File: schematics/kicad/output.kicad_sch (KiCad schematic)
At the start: 9 parts, among them U1 BT458, U2 HM53461, U3 HM53461, U4 HM53461, U5 HM53461, U6 HM53461, U7 HM53461, U8 HM53461, U9 HM53461

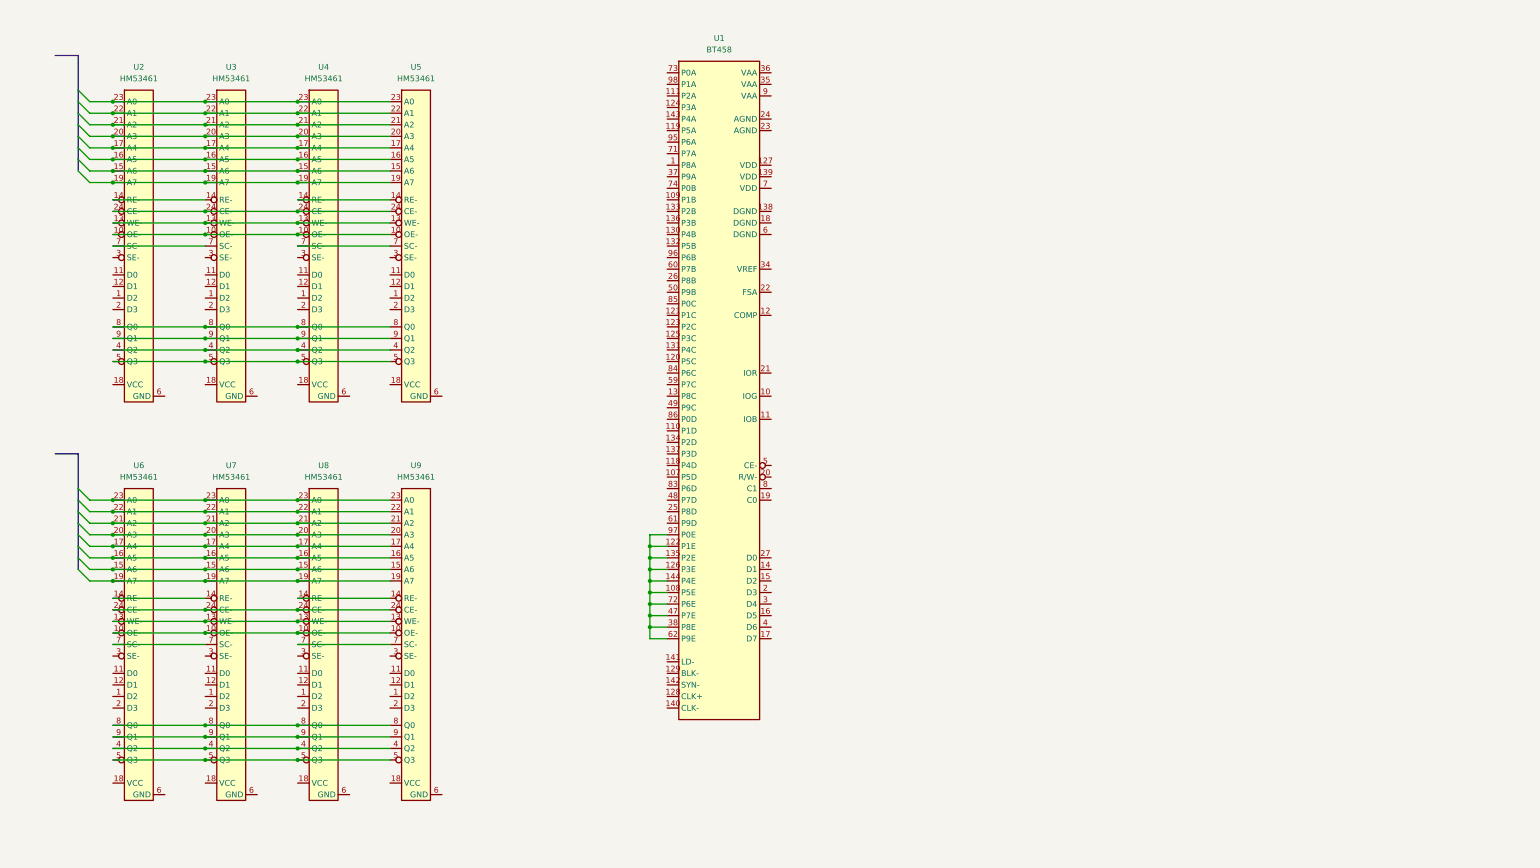
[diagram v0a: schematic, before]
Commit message: Fill in more output section
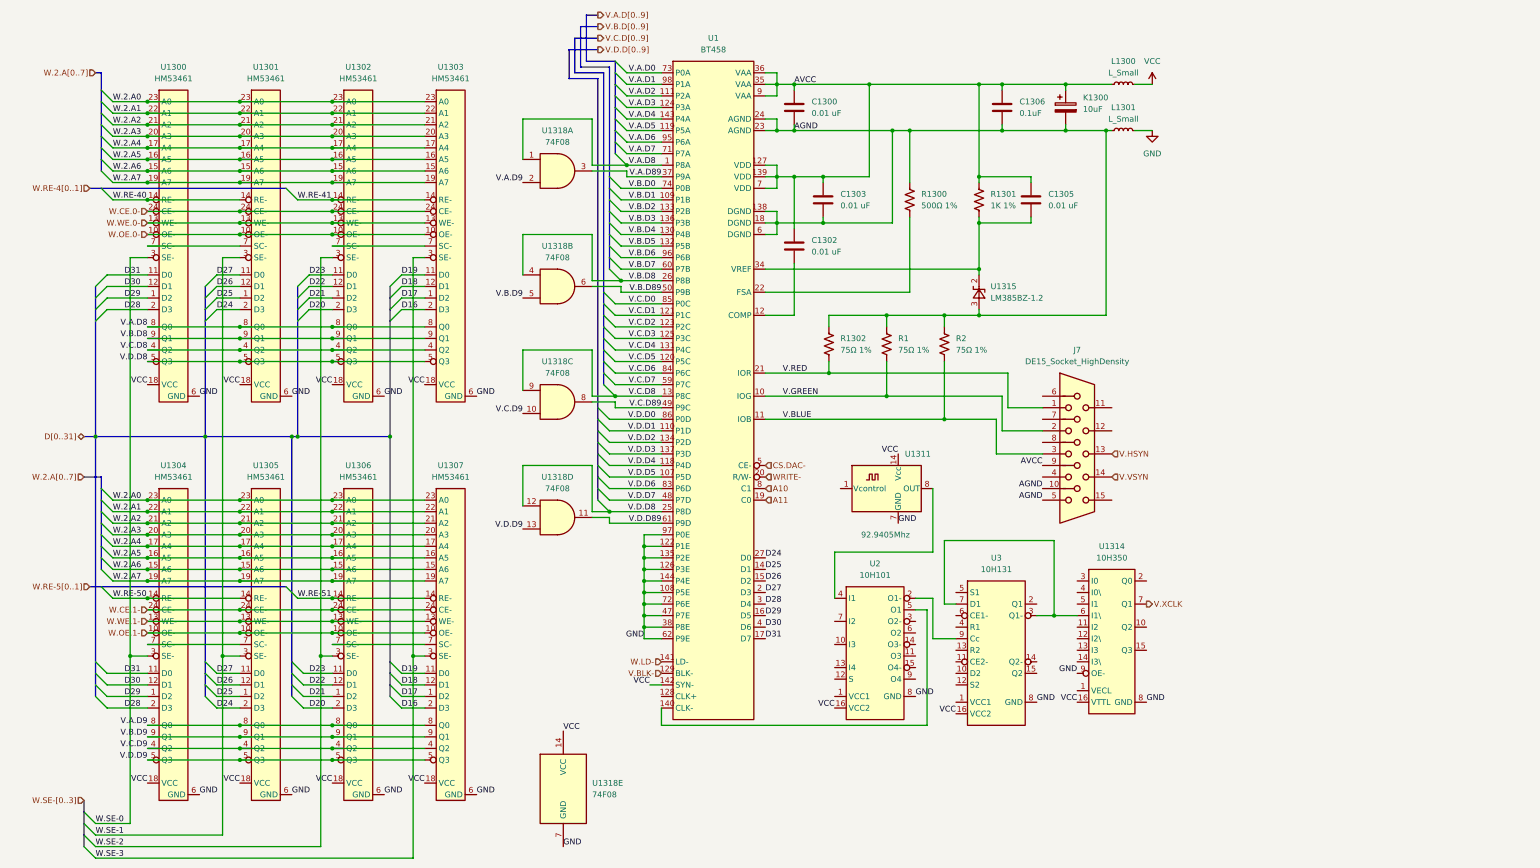
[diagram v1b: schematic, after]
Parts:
- added C1300, C1302, C1303, C1305: 0.01 uF, symbol Device:C
- added C1306: 0.1uF, symbol Device:C
- added J7: DE15_Socket_HighDensity, symbol Connector:DE15_Socket_HighDensity
- added K1300: 10uF, symbol Device:C_Polarized
- added L1300, L1301: L_Small, symbol Device:L_Small
- added R1, R1302, R2: 75Ω 1%, symbol Device:R_US
- added R1300: 500Ω 1%, symbol Device:R_US
- added R1301: 1K 1%, symbol Device:R_US
- added U1311: 92.9405Mhz, Oscillator:Oscillator_DIP-14, symbol Oscillator:OCXO-14
- added U1314: 10H350, Package_DIP:DIP-16_W7.62mm, symbol cg4:10H350
- added U1315: LM385BZ-1.2, Package_TO_SOT_THT:TO-92_Inline, symbol Reference_Voltage:LM385BZ-1.2
- added U1318: 74F08, symbol 74xx:74LS08
- added U2: 10H101, Package_DIP:DIP-16_W7.62mm, symbol cg4:10H101
- added U3: 10H131, Package_DIP:DIP-16_W7.62mm, symbol cg4:10H131
- renumbered U2 to U1300, U3 to U1301, U4 to U1302, U5 to U1303, U6 to U1304, U7 to U1305, U8 to U1306, U9 to U1307
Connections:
- net D25: now reaches U1305.1 (D2)
- net D25: now also U1.14 (D1), U1301.1 (D2)
- net W.OE.1-: now reaches U1304.10 (OE-), U1305.10 (OE-), U1306.10 (OE-), U1307.10 (OE-)
- net D27: now reaches U1305.11 (D0)
- net D27: now also U1.2 (D3), U1301.11 (D0)
- net D26: now reaches U1305.12 (D1)
- net D26: now also U1.15 (D2), U1301.12 (D1)
- net W.WE.1-: now reaches U1304.13 (WE-), U1305.13 (WE-), U1306.13 (WE-), U1307.13 (WE-)
- net W.RE-50: now reaches U1304.14 (RE-), U1305.14 (RE-)
- net W.2.A6: now reaches U1304.15 (A6), U1305.15 (A6), U1306.15 (A6), U1307.15 (A6)
- net W.2.A6: now also U1300.15 (A6), U1301.15 (A6), U1302.15 (A6), U1303.15 (A6)
- net W.2.A5: now reaches U1304.16 (A5), U1305.16 (A5), U1306.16 (A5), U1307.16 (A5)
- net W.2.A5: now also U1300.16 (A5), U1301.16 (A5), U1302.16 (A5), U1303.16 (A5)
- net W.2.A4: now reaches U1304.17 (A4), U1305.17 (A4), U1306.17 (A4), U1307.17 (A4)
- net W.2.A4: now also U1300.17 (A4), U1301.17 (A4), U1302.17 (A4), U1303.17 (A4)
- net VCC: now reaches U1305.18 (VCC)
- net VCC: now also U1.142 (SYN-), U1300.18 (VCC), U1301.18 (VCC), U1302.18 (VCC), U1303.18 (VCC), U1304.18 (VCC), U1306.18 (VCC), U1307.18 (VCC), L1300.2, U1311.14 (Vcc), U1314.16 (VTTL), U1318.14 (VCC), U2.16 (VCC2), U3.16 (VCC2)
- net W.2.A7: now reaches U1304.19 (A7), U1305.19 (A7), U1306.19 (A7), U1307.19 (A7)
- net W.2.A7: now also U1300.19 (A7), U1301.19 (A7), U1302.19 (A7), U1303.19 (A7)
- net D24: now reaches U1305.2 (D3)
- net D24: now also U1.27 (D0), U1301.2 (D3)
- net W.2.A3: now reaches U1304.20 (A3), U1305.20 (A3), U1306.20 (A3), U1307.20 (A3)
- net W.2.A3: now also U1300.20 (A3), U1301.20 (A3), U1302.20 (A3), U1303.20 (A3)
- net W.2.A2: now reaches U1304.21 (A2), U1305.21 (A2), U1306.21 (A2), U1307.21 (A2)
- net W.2.A2: now also U1300.21 (A2), U1301.21 (A2), U1302.21 (A2), U1303.21 (A2)
- net W.2.A1: now reaches U1304.22 (A1), U1305.22 (A1), U1306.22 (A1), U1307.22 (A1)
- net W.2.A1: now also U1300.22 (A1), U1301.22 (A1), U1302.22 (A1), U1303.22 (A1)
- net W.2.A0: now reaches U1304.23 (A0), U1305.23 (A0), U1306.23 (A0), U1307.23 (A0)
- net W.2.A0: now also U1300.23 (A0), U1301.23 (A0), U1302.23 (A0), U1303.23 (A0)
- net W.CE.1-: now reaches U1304.24 (CE-), U1305.24 (CE-), U1306.24 (CE-), U1307.24 (CE-)
- net W.SE-1: now reaches U1305.3 (SE-)
- net W.SE-1: now also U1301.3 (SE-)
- net V.C.D9: now reaches U1304.4 (Q2), U1305.4 (Q2), U1306.4 (Q2), U1307.4 (Q2)
- net V.C.D9: now also U1318.10
- net V.D.D9: now reaches U1304.5 (Q3), U1305.5 (Q3), U1306.5 (Q3), U1307.5 (Q3)
- net V.D.D9: now also U1318.13
- net GND: now reaches U1305.6 (GND)
- net GND: now also U1.108 (P5E), U1.122 (P1E), U1.126 (P3E), U1.135 (P2E), U1.144 (P4E), U1.38 (P8E), U1.47 (P7E), U1.62 (P9E), U1.72 (P6E), U1.97 (P0E), U1300.6 (GND), U1301.6 (GND), U1302.6 (GND), U1303.6 (GND), U1304.6 (GND), U1306.6 (GND), U1307.6 (GND), L1301.2, U1311.7 (GND), U1314.8 (GND), U1314.9 (OE-), U1318.7 (GND), U2.8 (GND), U3.8 (GND)
- net V.A.D9: now reaches U1304.8 (Q0), U1305.8 (Q0), U1306.8 (Q0), U1307.8 (Q0)
- net V.A.D9: now also U1318.2
- net V.B.D9: now reaches U1304.9 (Q1), U1305.9 (Q1), U1306.9 (Q1), U1307.9 (Q1)
- net V.B.D9: now also U1318.5
- net D21: now reaches U1306.1 (D2)
- net D21: now also U1302.1 (D2)
- net D23: now reaches U1306.11 (D0)
- net D23: now also U1302.11 (D0)
- net D22: now reaches U1306.12 (D1)
- net D22: now also U1302.12 (D1)
- net W.RE-51: now reaches U1306.14 (RE-), U1307.14 (RE-)
- net D20: now reaches U1306.2 (D3)
- net D20: now also U1302.2 (D3)
- net W.SE-2: now reaches U1306.3 (SE-)
- net W.SE-2: now also U1302.3 (SE-)
- net V.A.D8: now reaches U1.1 (P8A)
- net V.A.D8: now also U1300.8 (Q0), U1301.8 (Q0), U1302.8 (Q0), U1303.8 (Q0), U1318.1
- net V.GREEN: now reaches U1.10 (IOG)
- net V.GREEN: now also J7.2, R1.2
- net V.D.D5: now reaches U1.107 (P5D)
- net V.B.D1: now reaches U1.109 (P1B)
- net V.BLUE: now reaches U1.11 (IOB)
- net V.BLUE: now also J7.3, R2.2
- net V.D.D1: now reaches U1.110 (P1D)
- net V.A.D2: now reaches U1.111 (P2A)
- net V.D.D4: now reaches U1.118 (P4D)
- net V.A.D5: now reaches U1.119 (P5A)
- net at U1.12 (COMP): now also C1302.2
- net V.C.D5: now reaches U1.120 (P5C)
- net V.C.D1: now reaches U1.121 (P1C)
- net V.C.D2: now reaches U1.123 (P2C)
- net V.A.D3: now reaches U1.124 (P3A)
- net V.C.D3: now reaches U1.125 (P3C)
- net AVCC: now reaches U1.127 (VDD)
- net AVCC: now also U1.139 (VDD), U1.35 (VAA), U1.36 (VAA), U1.7 (VDD), U1.9 (VAA), C1300.1, C1302.1, C1303.1, C1305.1, C1306.1, J7.9, K1300.1, L1300.1, R1301.1
- net V.BLK-: now reaches U1.129 (BLK-)
- net V.C.D8: now reaches U1.13 (P8C)
- net V.C.D8: now also U1300.4 (Q2), U1301.4 (Q2), U1302.4 (Q2), U1303.4 (Q2), U1318.9
- net V.B.D4: now reaches U1.130 (P4B)
- net V.C.D4: now reaches U1.131 (P4C)
- net V.B.D5: now reaches U1.132 (P5B)
- net V.B.D2: now reaches U1.133 (P2B)
- net V.D.D2: now reaches U1.134 (P2D)
- net V.B.D3: now reaches U1.136 (P3B)
- net V.D.D3: now reaches U1.137 (P3D)
- net AGND: now reaches U1.138 (DGND)
- net AGND: now also U1.18 (DGND), U1.23 (AGND), U1.24 (AGND), U1.6 (DGND), C1300.2, C1303.2, C1306.2, J7.10, J7.5, K1300.2, L1301.1, R1.1, R1300.1, R1302.1, R2.1, U1315.3 (A)
- net at U1.140 (CLK-): now also U2.5 (O1)
- net W.LD-: now reaches U1.141 (LD-)
- net V.A.D4: now reaches U1.143 (P4A)
- net D29: now reaches U1.16 (D5)
- net D29: now also U1300.1 (D2), U1304.1 (D2)
- net D31: now reaches U1.17 (D7)
- net D31: now also U1300.11 (D0), U1304.11 (D0)
- net A11: now reaches U1.19 (C0)
- net WRITE-: now reaches U1.20 (R/W-)
- net V.RED: now reaches U1.21 (IOR)
- net V.RED: now also J7.1, R1302.2
- net at U1.22 (FSA): now also R1300.2
- net V.D.D8: now reaches U1.25 (P8D)
- net V.D.D8: now also U1300.5 (Q3), U1301.5 (Q3), U1302.5 (Q3), U1303.5 (Q3), U1318.12
- net V.B.D8: now reaches U1.26 (P8B)
- net V.B.D8: now also U1300.9 (Q1), U1301.9 (Q1), U1302.9 (Q1), U1303.9 (Q1), U1318.4
- net D28: now reaches U1.3 (D4)
- net D28: now also U1300.2 (D3), U1304.2 (D3)
- net at U1.34 (VREF): now also C1305.2, R1301.2, U1315.2 (K)
- net V.A.D89: now reaches U1.37 (P9A)
- net V.A.D89: now also U1318.3
- net D30: now reaches U1.4 (D6)
- net D30: now also U1300.12 (D1), U1304.12 (D1)
- net V.D.D7: now reaches U1.48 (P7D)
- net V.C.D89: now reaches U1.49 (P9C)
- net V.C.D89: now also U1318.8
- net CS.DAC-: now reaches U1.5 (CE-)
- net V.B.D89: now reaches U1.50 (P9B)
- net V.B.D89: now also U1318.6
- net V.C.D7: now reaches U1.59 (P7C)
- net V.B.D7: now reaches U1.60 (P7B)
- net V.D.D89: now reaches U1.61 (P9D)
- net V.D.D89: now also U1318.11
- net V.A.D7: now reaches U1.71 (P7A)
- net V.A.D0: now reaches U1.73 (P0A)
- net V.B.D0: now reaches U1.74 (P0B)
- net A10: now reaches U1.8 (C1)
- net V.D.D6: now reaches U1.83 (P6D)
- net V.C.D6: now reaches U1.84 (P6C)
- net V.C.D0: now reaches U1.85 (P0C)
- net V.D.D0: now reaches U1.86 (P0D)
- net V.A.D6: now reaches U1.95 (P6A)
- net V.B.D6: now reaches U1.96 (P6B)
- net V.A.D1: now reaches U1.98 (P1A)
- net W.SE-0: now reaches U1304.3 (SE-)
- net W.SE-0: now also U1300.3 (SE-)
- net D17: now reaches U1303.1 (D2)
- net D17: now also U1307.1 (D2)
- net W.OE.0-: now reaches U1300.10 (OE-), U1301.10 (OE-), U1302.10 (OE-), U1303.10 (OE-)
- net D19: now reaches U1303.11 (D0)
- net D19: now also U1307.11 (D0)
- net D18: now reaches U1303.12 (D1)
- net D18: now also U1307.12 (D1)
- net W.WE.0-: now reaches U1300.13 (WE-), U1301.13 (WE-), U1302.13 (WE-), U1303.13 (WE-)
- net W.RE-41: now reaches U1302.14 (RE-), U1303.14 (RE-)
- net D16: now reaches U1303.2 (D3)
- net D16: now also U1307.2 (D3)
- net W.CE.0-: now reaches U1300.24 (CE-), U1301.24 (CE-), U1302.24 (CE-), U1303.24 (CE-)
- net W.SE-3: now reaches U1303.3 (SE-)
- net W.SE-3: now also U1307.3 (SE-)
- net W.RE-40: now reaches U1300.14 (RE-), U1301.14 (RE-)
- new net: U1311.8 (OUT), U2.4 (I1)
- new net: U2.2 (O1-), U3.9 (Cc)
- new net: U1314.6 (I1\), U3.3 (Q1-), U3.7 (D1)
- new net V.HSYN: J7.13
- new net V.VSYN: J7.14
- new net V.XCLK: U1314.7 (Q1)
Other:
- moved on the sheet: U1, U1300, U1301, U1302, U1303, U1304, U1305, U1306, U1307

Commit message: Populate misc page with P4 connector and caps Finish MUX, RAM and most of Output Lots of progress on Control Lay out root and connect most components
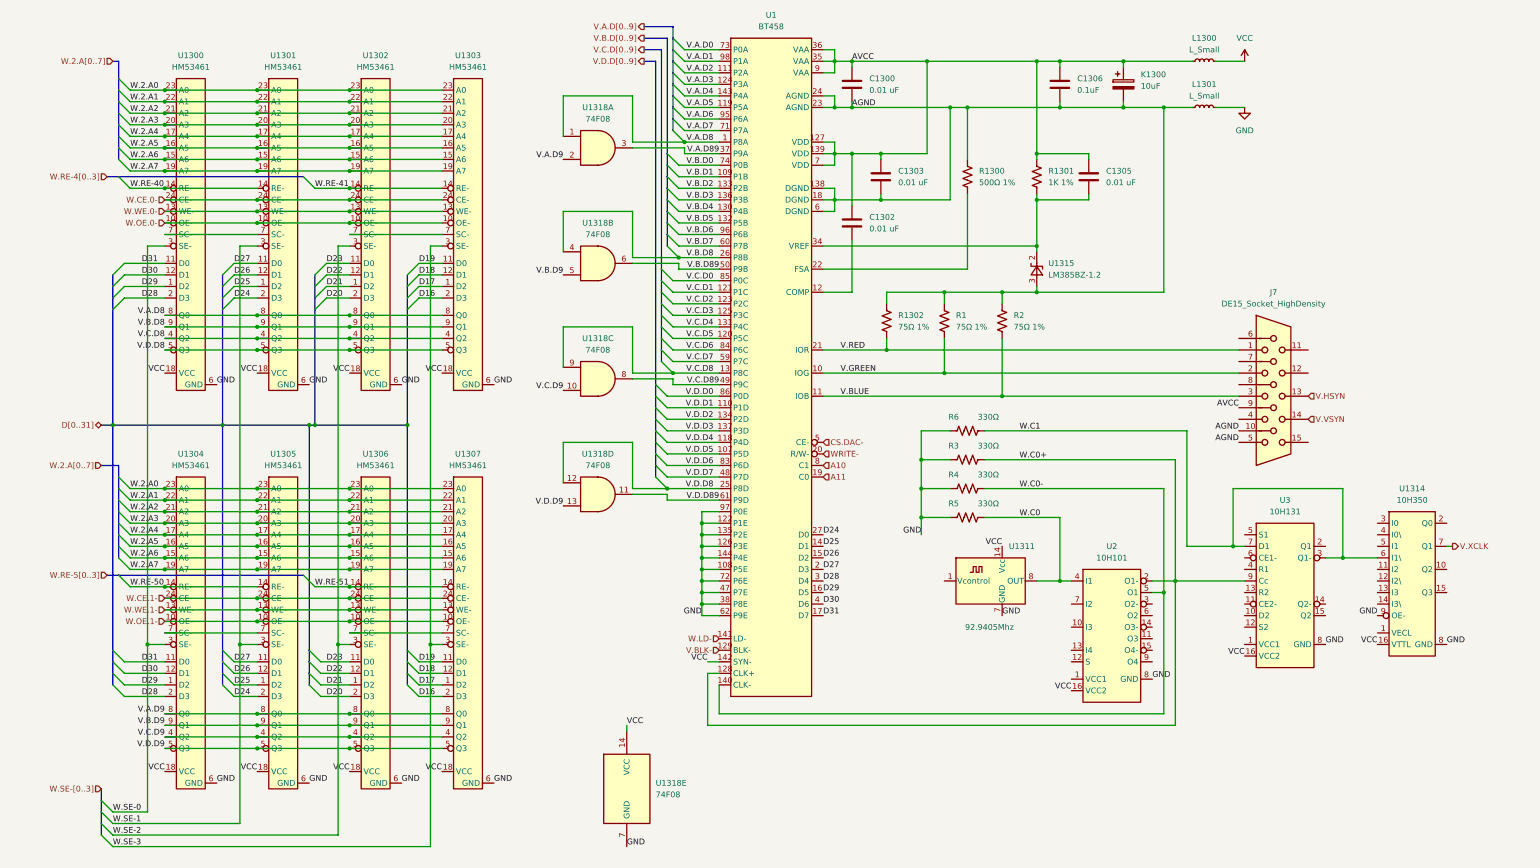
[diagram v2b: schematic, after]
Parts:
- added R3, R4, R5, R6: 330Ω, symbol Device:R_US
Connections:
- net GND: now also R3.1, R4.1, R5.1, R6.1
- net W.C0+: now reaches U1.128 (CLK+)
- net W.C0+: now also U2.2 (O1-), U3.9 (Cc), R3.2
- net W.C0-: now reaches U1.140 (CLK-), U2.5 (O1)
- net W.C0-: now also R4.2
- net W.C0: now reaches U1311.8 (OUT), U2.4 (I1)
- net W.C0: now also R5.2
- net W.C1: now reaches U1314.6 (I1\), U3.3 (Q1-), U3.7 (D1)
- net W.C1: now also R6.2
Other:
- moved on the sheet: C1300, C1302, C1303, C1305, C1306, J7, K1300, L1300, L1301, R1, R1300, R1301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

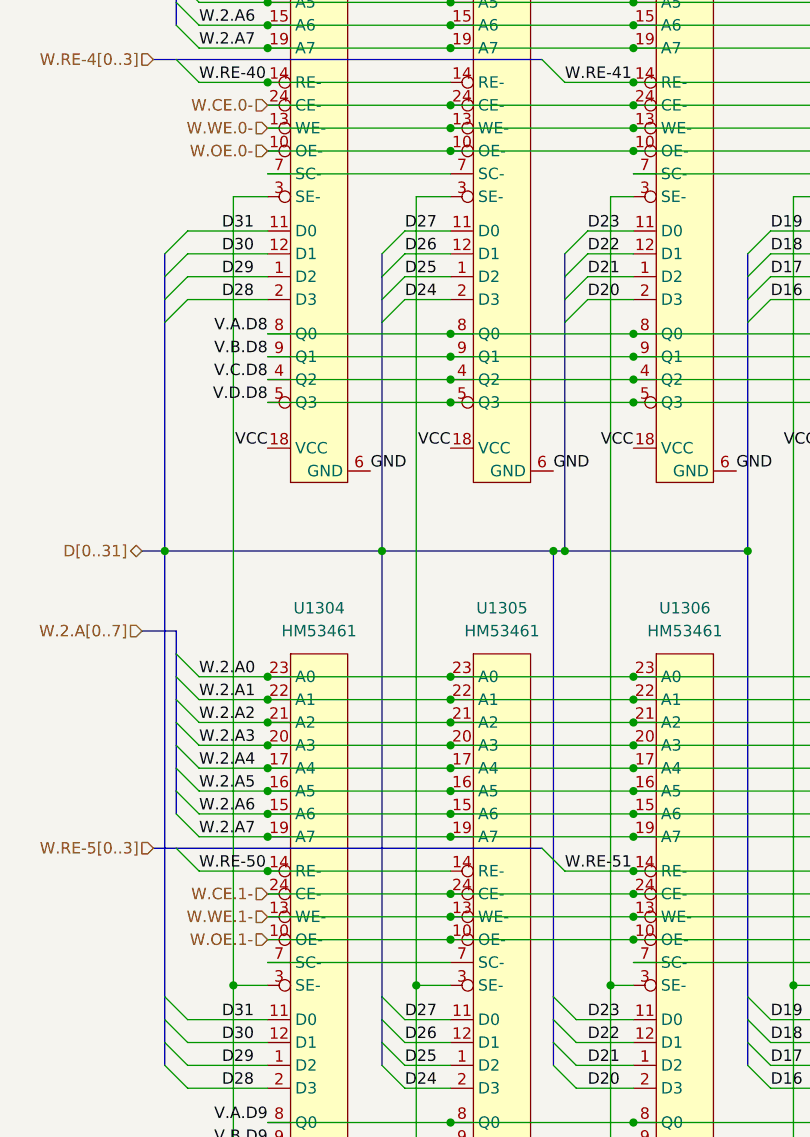
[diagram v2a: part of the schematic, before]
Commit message: Fill in most of control, wire up addresses, and more
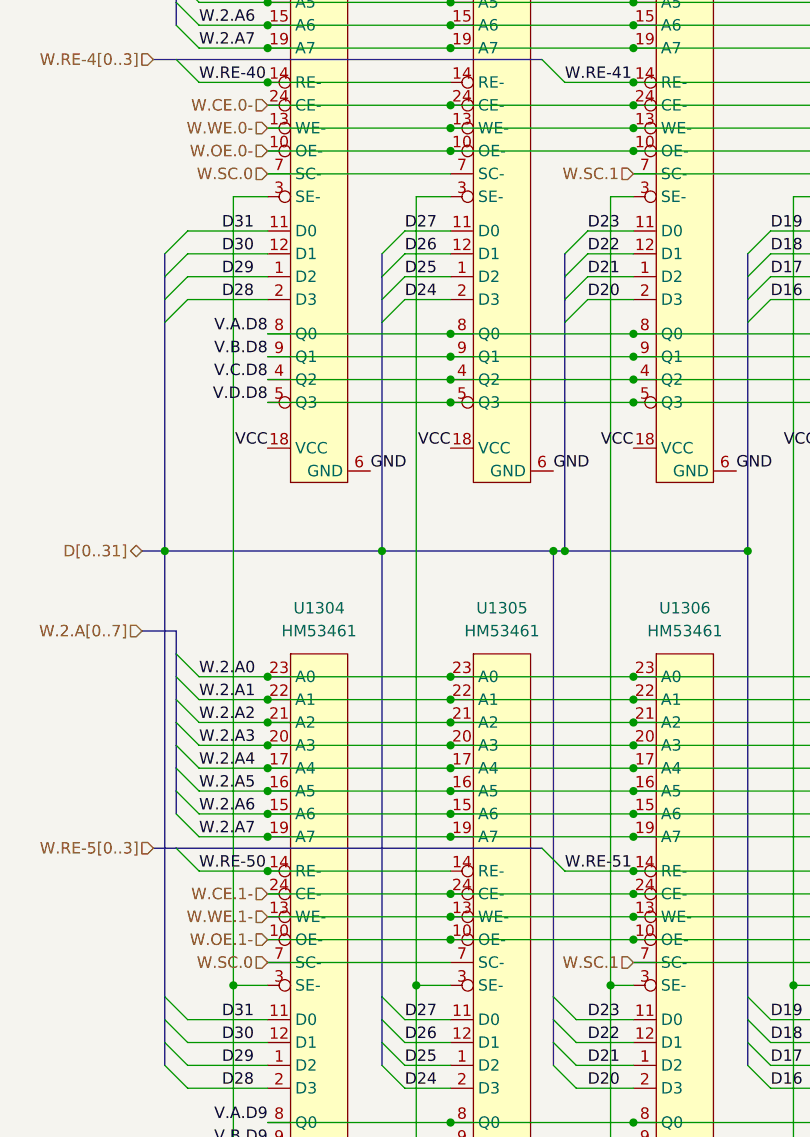
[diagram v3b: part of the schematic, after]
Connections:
- net W.SC.0: now reaches U1304.7 (SC-), U1305.7 (SC-)
- net W.SC.0: now also U1300.7 (SC-), U1301.7 (SC-)
- net W.SC.1: now reaches U1306.7 (SC-), U1307.7 (SC-)
- net W.SC.1: now also U1302.7 (SC-), U1303.7 (SC-)
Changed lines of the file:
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@@
+		)
+	)
+	(hierarchical_label "W.SC.1"
+		(shape input)
+		(at 83.82 62.23 180)
+		(effects
+			(font
+				(size 1.27 1.27)
+			)
+			(justify right)
 		)
 	)
@@
 		)
 	)
+	(hierarchical_label "W.SC.0"
+		(shape input)
+		(at 43.18 62.23 180)
+		(effects
+			(font
+				(size 1.27 1.27)
+			)
+			(justify right)
+		)
+	)
 	(hierarchical_label "W.2.A[0..7]"
 		(shape input)
@@
 		)
 	)
+	(hierarchical_label "W.SC.1"
+		(shape input)
+		(at 83.82 149.86 180)
+		(effects
+			(font
+				(size 1.27 1.27)
+			)
+			(justify right)
+		)
+	)
 	(hierarchical_label "V.B.D[0..9]"
 		(shape output)
@@
 		(effects
 			(font
+				(size 1.27 1.27)
+			)
+			(justify right)
+		)
+	)
+	(hierarchical_label "W.SC.0"
+		(shape input)
+		(at 43.18 149.86 180)
+		(effects
+			(font
